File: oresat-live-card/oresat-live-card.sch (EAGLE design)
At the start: 275 parts, among them J1 ORESAT-DEBUG-CONNECTOR-CARD, J100 DM3BT-DSF-PEJS, J102 FTSH-105-XX-X-DV-K, J4 TFM-120-01-L-D-RA, Q1 MMBT2907, Q2 PMV45EN, Q3 DMP2240UDM, Q4 PMV45EN, Q5 MOSFET-PCH-SOT23-6, Q6 MOSFET-PCH-SOT23-6, U1 RCLAMP0504FB, U10 TLVH431, U11 TCAN330, U12 MIC842LYC5, U13 MIC842LYC5, U14 MAX4211FETE, U15 TPS62112, U16 MAX7310ATE, U17 25AAXX, U18 RCLAMP0504FB, U2 TPS2051CDBVR, U4 SN74LVC1G07DCK, U7 OSD3358-512M-BSM, Y1 24MHz, Y2 ABS07-32.768KHZ-T

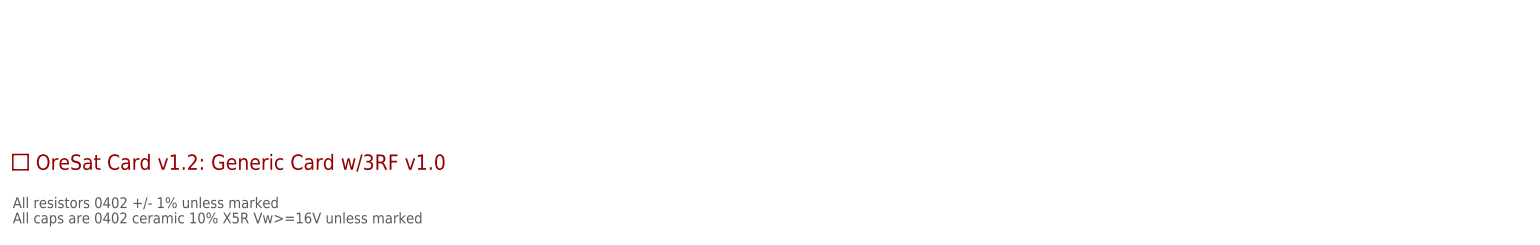
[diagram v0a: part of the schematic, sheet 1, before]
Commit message: Checking in dxwifi with the latest card outline. but, it's the old v1.0. So it needs to be re-done one more time :(
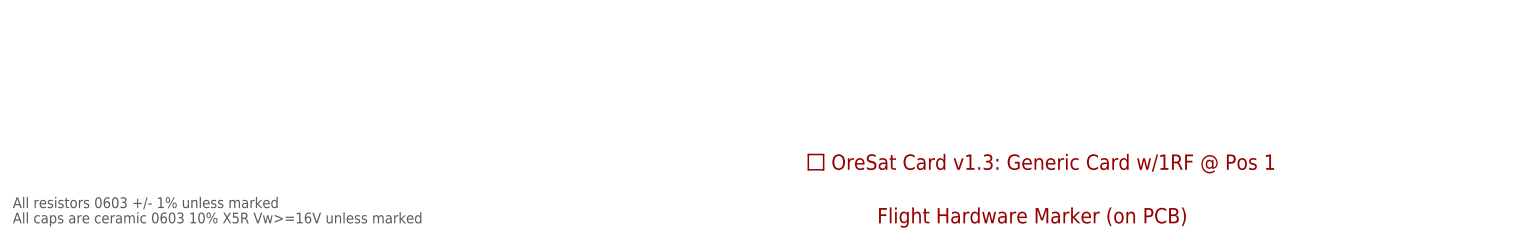
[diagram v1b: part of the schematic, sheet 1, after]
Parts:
- added U$1: FLIGHMARKERNEW, oresat-flight-marker:FLIGHMARKERNEW
- PCB1: value ORESAT-CARD-V1.2-GENERIC-3XRF-V1.0 -> ORESAT-CARD-V1.3-GENERIC-1RF-POS1; device oresat-cards:ORESAT-CARD-V1.2-GENERIC-3XRF-V1.0 -> oresat-cards:ORESAT-CARD-V1.3-GENERIC-1RF-POS1
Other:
- note added: "All caps are ceramic 0603 10% X5R Vw>=16V unless marked"
- note added: "All resistors 0603 +/- 1% unless marked"
- note removed: "All caps are 0402 ceramic 10% X5R Vw>=16V unless marked"
- note removed: "All resistors 0402 +/- 1% unless marked"
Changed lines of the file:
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@@
 <?xml version="1.0" encoding="utf-8"?>
 <!DOCTYPE eagle SYSTEM "eagle.dtd">
-<eagle version="9.6.2">
+<eagle version="9.6.1">
 <drawing>
 <settings>
@@
 <setting verticaltext="up"/>
 </settings>
-<grid distance="0.05" unitdist="inch" unit="inch" style="lines" multiple="1" display="no" altdistance="0.01" altunitdist="inch" altunit="inch"/>
+<grid distance="0.1" unitdist="inch" unit="inch" style="lines" multiple="1" display="no" altdistance="0.01" altunitdist="inch" altunit="inch"/>
 <layers>
 <layer number="1" name="Top" color="4" fill="1" visible="no" active="no"/>
@@
 <part name="R74" library="oresat-rcl" deviceset="R-US_" device="0603-A" value="100"/>
 <part name="R75" library="oresat-rcl" deviceset="R-US_" device="0603-A" value="100"/>
-<part name="PCB1" library="oresat-cards" deviceset="ORESAT-CARD-V1.2-GENERIC-3XRF-V1.0" device=""/>
+<part name="PCB1" library="oresat-cards" deviceset="ORESAT-CARD-V1.3-GENERIC-1RF-POS1" device=""/>
+<part name="U$1" library="oresat-flight-marker" deviceset="FLIGHMARKER" device="NEW"/>
 </parts>
 <sheets>
@@
 <text x="341.63" y="26.67" size="3.81" layer="94">OreSat Live Card</text>
 <text x="416.56" y="6.35" size="3.81" layer="94">0.1</text>
-<text x="11.43" y="5.08" size="1.778" layer="97">All resistors 0402 +/- 1% unless marked</text>
-<text x="11.43" y="2.54" size="1.778" layer="97">All caps are 0402 ceramic 10% X5R Vw&gt;=16V unless marked</text>
+<text x="11.43" y="5.08" size="1.778" layer="97">All resistors 0603 +/- 1% unless marked</text>
+<text x="11.43" y="2.54" size="1.778" layer="97">All caps are ceramic 0603 10% X5R Vw&gt;=16V unless marked</text>
 <wire x1="99.06" y1="236.22" x2="205.74" y2="236.22" width="0.1524" layer="97"/>
 <wire x1="205.74" y1="236.22" x2="205.74" y2="114.3" width="0.1524" layer="97"/>
@@
 <attribute name="VALUE" x="129.54" y="165.354" size="1.778" layer="96" align="bottom-center"/>
 </instance>
-<instance part="PCB1" gate="G$1" x="12.7" y="12.7" smashed="yes"/>
+<instance part="PCB1" gate="G$1" x="144.78" y="12.7" smashed="yes"/>
+<instance part="U$1" gate="G$1" x="154.94" y="2.54" smashed="yes"/>
 </instances>
 <busses>

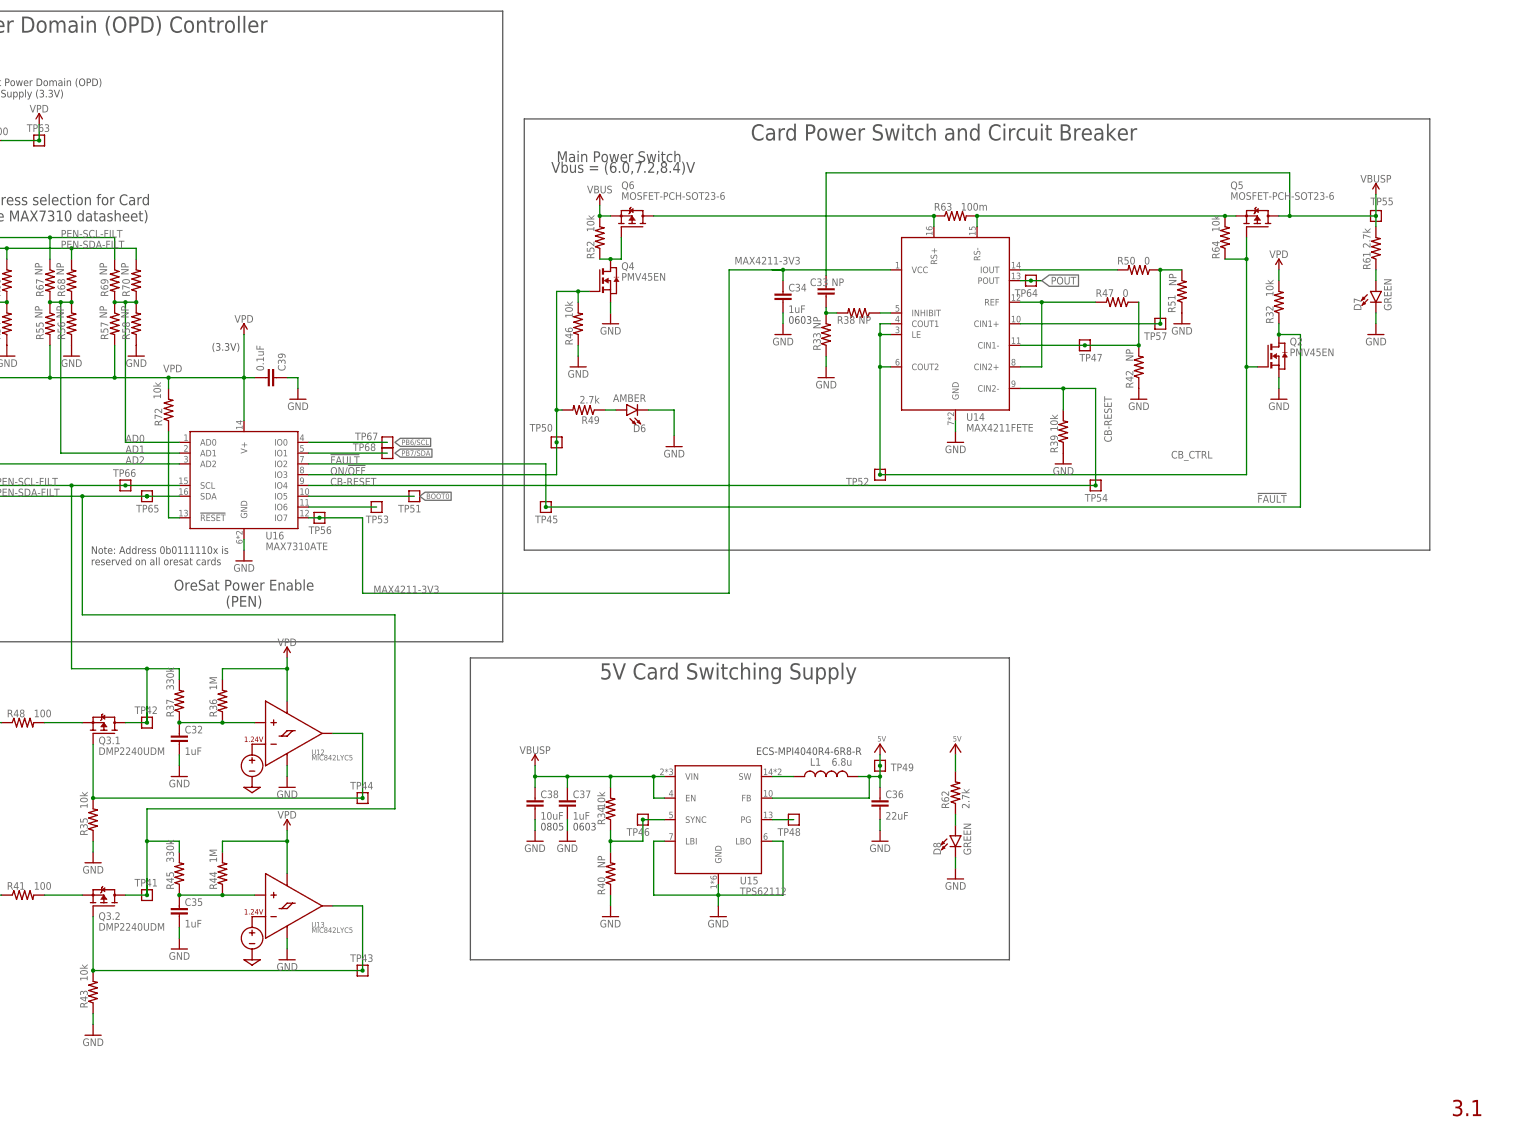
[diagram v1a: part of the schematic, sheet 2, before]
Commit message: Third time is the charm? Started with Star Tracker v1.2, added new card outline, moved out all extraneaous stuff, added RF connectors.
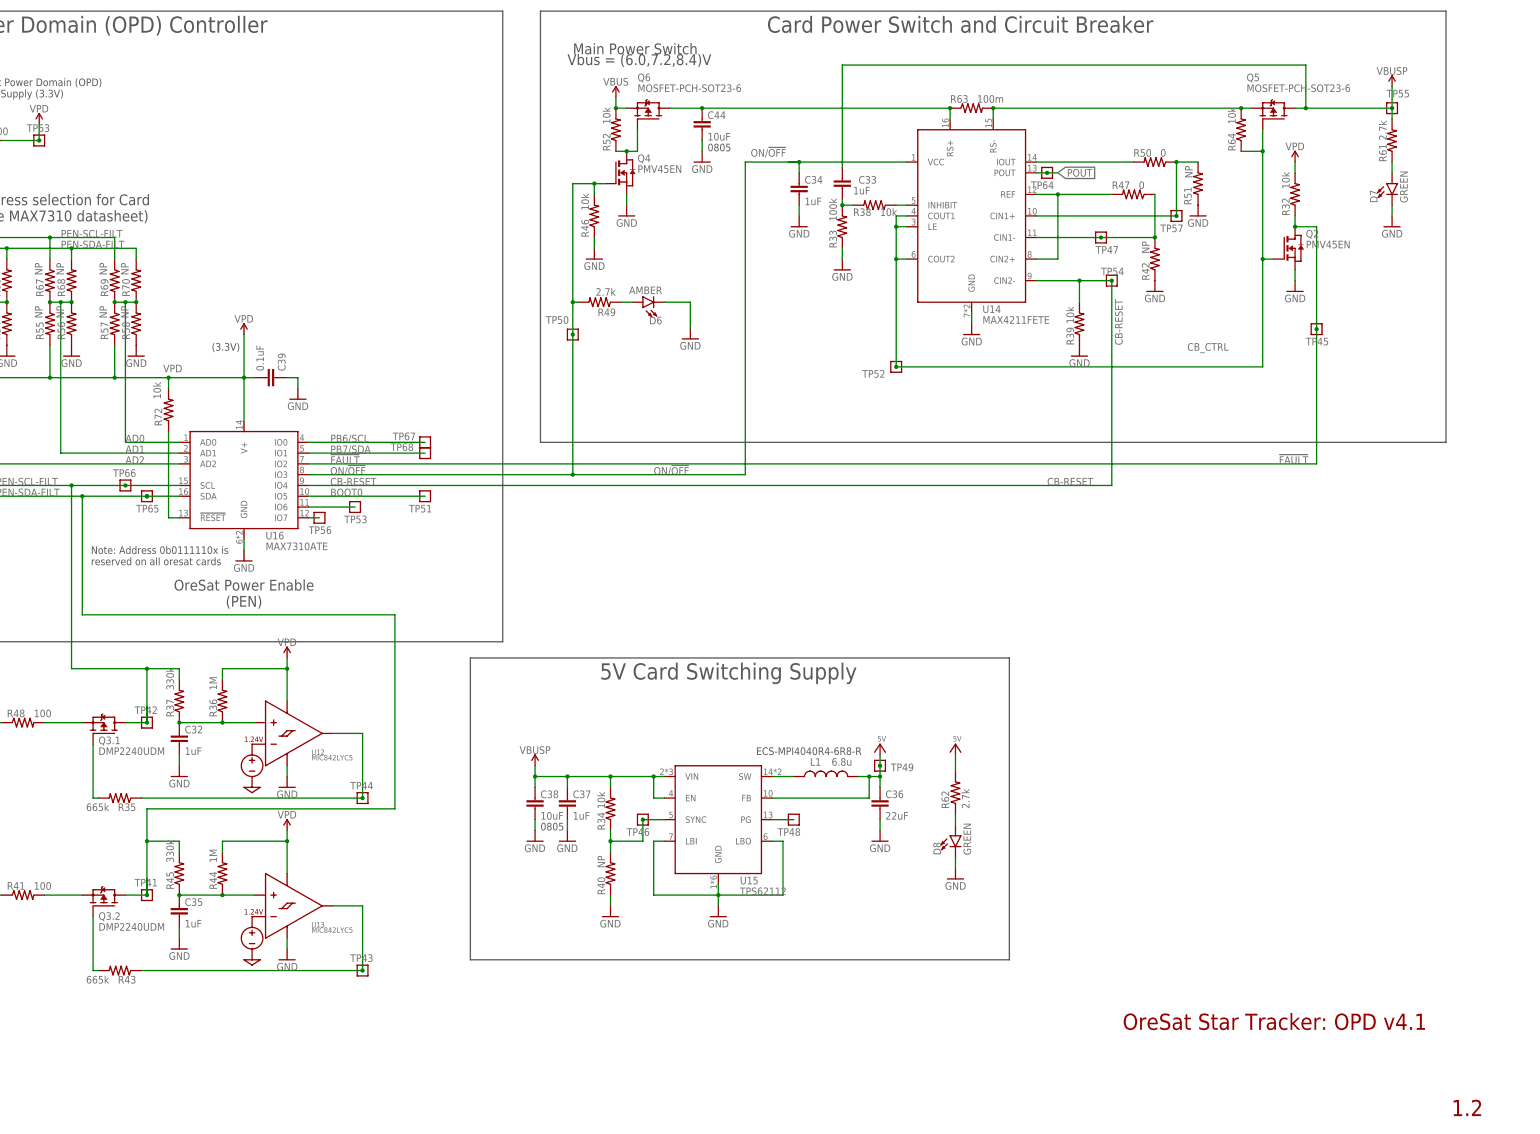
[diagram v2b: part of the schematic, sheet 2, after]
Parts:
- added C44: 10uF, oresat-rcl:C-EU0805-B
- added CM1: J-MOLEX-SMPM-73300-003X, J-Molex-73300-003X-SMPM-M-edge-mount:J-MOLEX-SMPM-73300-003X
- added U$2: U.FL-R-SMA, J-HRS-U.FL-R-SMT-1(10)-M-RF:U.FL-R-SMA
- C33: value NP -> 1uF
- R33: value NP -> 100k
- R35, R43: value 10k -> 665k
- R38: value NP -> 10k
- U3: value (none) -> THGBMJG7C2LBAU8
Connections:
- removed net D0_I: JP102.1
- removed net D10_I: U7C.MCASP0_AXR1
- removed net D11_I: U7C.MCASP0_AHCLKX
- removed net D1_I: JP103.1
- removed net D2_I: JP110.1
- removed net D3_I: JP111.1
- removed net D4_I: U7C.MCASP0_ACLKX
- removed net D5_I: U7C.MCASP0_FSX
- removed net D6_I: U7C.MCASP0_AXR0
- removed net D7_I: U7C.MCASP0_AHCLKR
- removed net D8_I: U7C.MCASP0_ACLKR
- removed net D9_I: U7C.MCASP0_FSR
- removed net HSYNC_I: U7C.GPMC_AD15
- removed net MAX4211-3V3: C34.1, TP56.1, U14.VCC, U16.IO7
- removed net PIXCLK_I: U7C.XDMA_EVENT_INTR1
- removed net VSYNC_I: U7C.GPMC_AD14
- new net N$113: Q3.2.G, R43.2
- new net N$117: Q3.1.G, R35.2
- new net N$19: CM1.CENTER, U$2.P$1
- new net N$32: TP56.1, U16.IO7
- net GND: now also C44.2, CM1.SHIELD, CM1.SHIELD1, CM1.SHIELD2, CM1.SHIELD3, U$2.P$2; no longer R35.1, R43.1
- net N$27: now also R35.1; no longer Q3.1.G, R35.2
- net N$580: now also R43.1; no longer Q3.2.G, R43.2
- net N$98: now also C44.1
- net ON/!OFF: now also C34.1, U14.VCC
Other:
- note added: "1.2"
- note added: "All caps are 0402 ceramic 10% X5R Vw>=16V unless marked"
- note added: "All resistors 0402 +/- 1% unless marked"
- note added: "OreSat Star Tracker: Camera, eMMC"
- note added: "OreSat Star Tracker: Connectors"
- note added: "OreSat Star Tracker: OPD v4.1"
- note added: "OreSat Star Tracker: OSD Power/Misc"
- note added: "OreSat Star Tracker: USB, JTAG, OSC"
- note removed: "0.1"
- note removed: "0603"
- note removed: "3.1"
- note removed: "All caps are ceramic 0603 10% X5R Vw>=16V unless marked"
- note removed: "All resistors 0603 +/- 1% unless marked"
- note removed: "OreSat Live Card"
- note removed: "Unfortunately MMC0 (SD card) and the PRU share 4 pins. We can get away without using them and just using the 8 highest bits of the camera parallel bus. However, since we will ultimately be booting off of eMMC, we could then utilize the 4 lowest bits. Likewise, populate once only the eMMc is used, cut these jumpers and connect them to the PRUs"
- moved on the sheet: C33, C34, D6, D7, Q2, Q4, Q5, Q6, R32, R33, R35, R38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

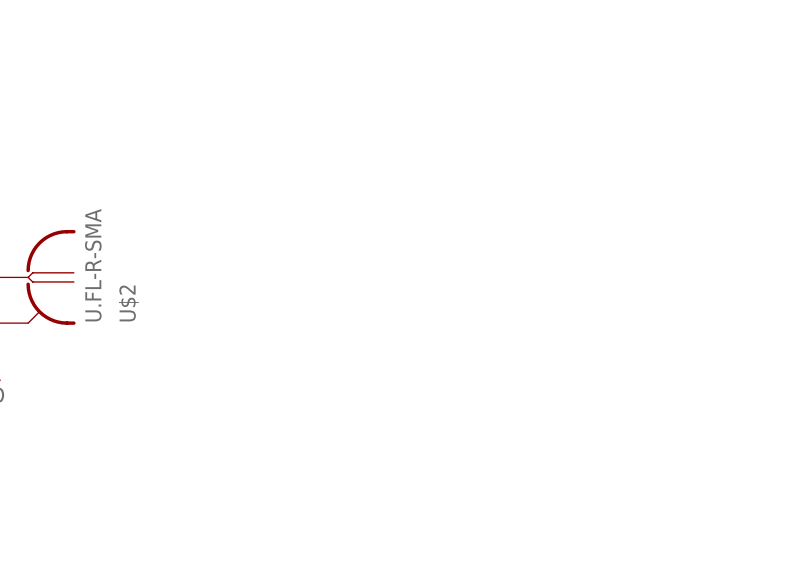
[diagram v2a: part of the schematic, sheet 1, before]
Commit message: Added and locked DXF layer from Emmy with OreSat live camera mount. Added lens cutout, added  TSTOP/TRESTRICT and bottom layers around hardware. Added WF board and 1mm connector. Ready for munging!
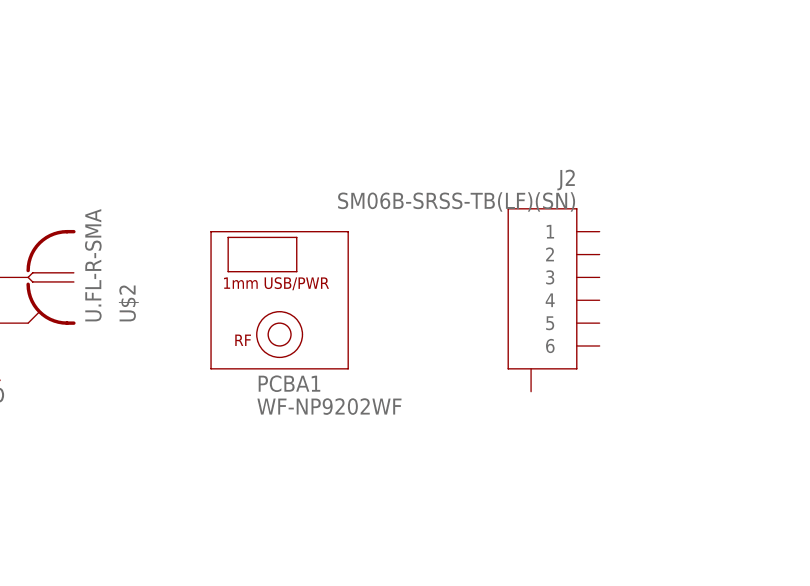
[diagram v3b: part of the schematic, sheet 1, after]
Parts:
- added J2: SM06B-SRSS-TB(LF)(SN), J-JST-SM06B-SRSS-TB(LF)(SN)-1mm-smt-6pin:SM06B-SRSS-TB(LF)(SN)
- added PCBA1: WF-NP9202WF, PCBA-WF-NP9202-wifi-adapter:WF-NP9202WF
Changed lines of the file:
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@@
 <part name="GND4" library="supply1" library_urn="urn:adsk.eagle:library:371" deviceset="GND" device=""/>
 <part name="GND5" library="supply1" library_urn="urn:adsk.eagle:library:371" deviceset="GND" device=""/>
+<part name="PCBA1" library="PCBA-WF-NP9202-wifi-adapter" deviceset="WF-NP9202" device="WF"/>
+<part name="J2" library="J-JST-SM06B-SRSS-TB(LF)(SN)-1mm-smt-6pin" deviceset="SM06B-SRSS-TB(LF)(SN)" device=""/>
 </parts>
 <sheets>
@@
 <instance part="GND5" gate="1" x="193.04" y="64.77" smashed="yes" rot="MR0">
 <attribute name="VALUE" x="195.58" y="62.23" size="1.778" layer="96" rot="MR0"/>
+</instance>
+<instance part="PCBA1" gate="G$1" x="226.06" y="73.66" smashed="yes">
+<attribute name="NAME" x="223.52" y="63.5" size="1.778" layer="95"/>
+<attribute name="VALUE" x="223.52" y="60.96" size="1.778" layer="96"/>
+</instance>
+<instance part="J2" gate="A" x="254" y="76.2" smashed="yes" rot="MR0">
+<attribute name="NAME" x="259.08" y="86.36" size="1.778" layer="95" ratio="6" rot="SMR0"/>
+<attribute name="VALUE" x="259.08" y="83.82" size="1.778" layer="96" ratio="20" rot="MR0"/>
 </instance>
 </instances>
@@
 </sheet>
 <sheet>
-<description>OSD3358 SD, eMMC, Camera, etc : SIP C, D</description>
+<description>OSD3358 SD, eMMC: SIP C, D</description>
 <plain>
 <text x="784.86" y="375.92" size="1.778" layer="97">SYSBOOT Jumper to config boot order
